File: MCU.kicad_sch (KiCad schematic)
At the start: 83 parts, among them J1 Conn_01x02_Pin, J11 Logger Connector, J12 UART Connector, J13 External UART, J14 External I2C, J15 JTAG Header, J2 Conn_01x02_Pin, J27 Conn_01x02_Pin, SW1 XRSn_button, U13 M24M01E-FMN6TP, U17 TRS3221EIPWR, U5 F280025PNS, Y2 H130B-16.000-18-3030-EXT-TR

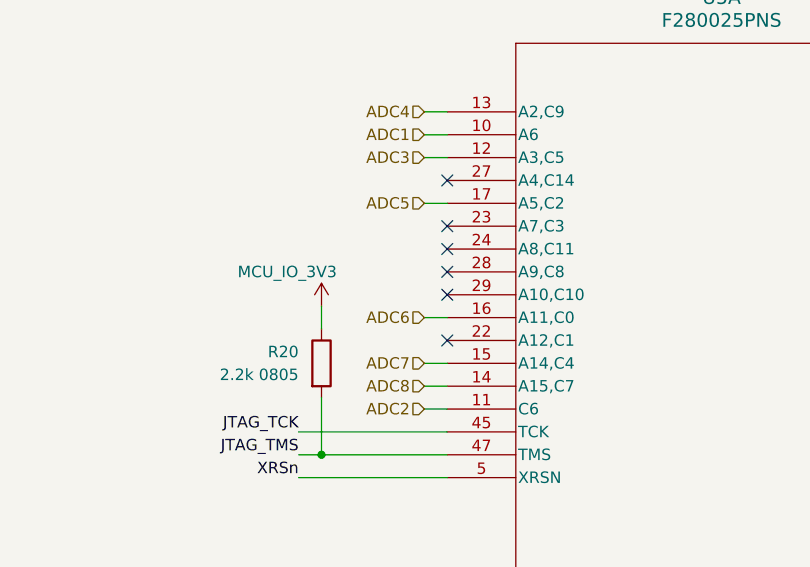
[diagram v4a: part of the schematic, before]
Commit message: re-arranged ADC channels, add voltage monitoring and connect remaining nets
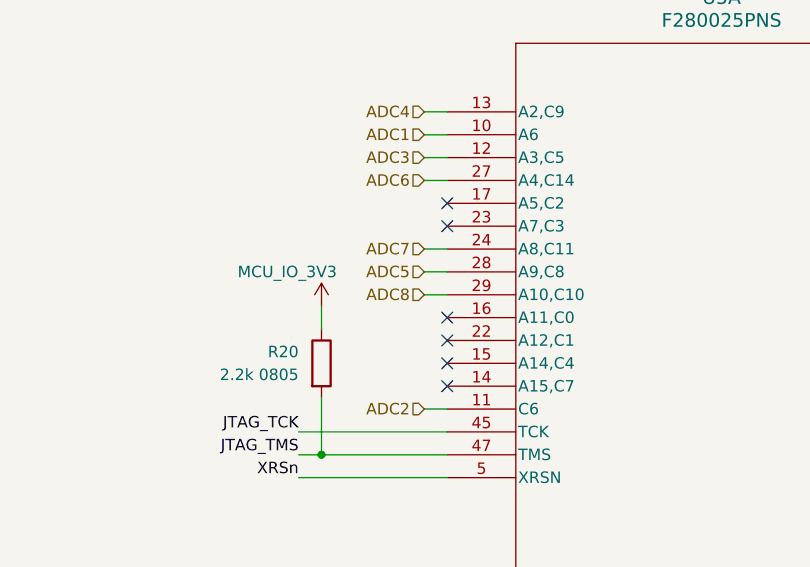
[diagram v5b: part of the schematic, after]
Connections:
- net ADC5: now also U5.28 (A9,C8); no longer U5.17 (A5,C2)
- net ADC6: now also U5.27 (A4,C14); no longer U5.16 (A11,C0)
- net ADC7: now also U5.24 (A8,C11); no longer U5.15 (A14,C4)
- net ADC8: now also U5.29 (A10,C10); no longer U5.14 (A15,C7)
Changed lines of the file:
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@@
 	)
 	(no_connect
-		(at 307.34 34.29)
+		(at 246.38 62.23)
 	)
 	(no_connect
-		(at 246.38 41.91)
+		(at 307.34 34.29)
 	)
 	(no_connect
@@
 	)
 	(no_connect
+		(at 246.38 64.77)
+	)
+	(no_connect
 		(at 97.79 208.28)
 	)
 	(no_connect
+		(at 246.38 44.45)
+	)
+	(no_connect
 		(at 246.38 59.69)
 	)
@@
 	)
 	(no_connect
-		(at 246.38 49.53)
+		(at 246.38 57.15)
 	)
 	(no_connect
@@
 	)
 	(no_connect
-		(at 246.38 52.07)
-	)
-	(no_connect
 		(at 307.34 36.83)
 	)
@@
 		(at 246.38 46.99)
 	)
-	(no_connect
-		(at 246.38 54.61)
-	)
 	(wire
 		(pts
@@
 	(wire
 		(pts
+			(xy 243.84 49.53) (xy 246.38 49.53)
+		)
+		(stroke
+			(width 0)
+			(type default)
+		)
+	)
+	(wire
+		(pts
 			(xy 170.18 48.26) (xy 175.26 48.26)
 		)
@@
 	(wire
 		(pts
+			(xy 243.84 41.91) (xy 246.38 41.91)
+		)
+		(stroke
+			(width 0)
+			(type default)
+		)
+	)
+	(wire
+		(pts
 			(xy 354.33 96.52) (xy 354.33 97.79)
 		)
@@
 	(wire
 		(pts
-			(xy 243.84 57.15) (xy 246.38 57.15)
-		)
-		(stroke
-			(width 0)
-			(type default)
-		)
-	)
-	(wire
-		(pts
 			(xy 180.34 256.54) (xy 190.5 256.54)
 		)
@@
 	(wire
 		(pts
-			(xy 243.84 44.45) (xy 246.38 44.45)
-		)
-		(stroke
-			(width 0)
-			(type default)
-		)
-	)
-	(wire
-		(pts
 			(xy 120.65 170.18) (xy 124.46 170.18)
 		)
@@
 	(wire
 		(pts
+			(xy 243.84 34.29) (xy 246.38 34.29)
+		)
+		(stroke
+			(width 0)
+			(type default)
+		)
+	)
+	(wire
+		(pts
 			(xy 307.34 74.93) (xy 309.88 74.93)
 		)
@@
 	(wire
 		(pts
+			(xy 243.84 52.07) (xy 246.38 52.07)
+		)
+		(stroke
+			(width 0)
+			(type default)
+		)
+	)
+	(wire
+		(pts
 			(xy 180.34 259.08) (xy 190.5 259.08)
 		)
@@
 	(wire
 		(pts
+			(xy 243.84 54.61) (xy 246.38 54.61)
+		)
+		(stroke
+			(width 0)
+			(type default)
+		)
+	)
+	(wire
+		(pts
 			(xy 307.34 118.11) (xy 309.88 118.11)
 		)
@@
 	(wire
 		(pts
-			(xy 243.84 62.23) (xy 246.38 62.23)
-		)
-		(stroke
-			(width 0)
-			(type default)
-		)
-	)
-	(wire
-		(pts
 			(xy 52.07 161.29) (xy 55.88 161.29)
 		)
@@
 	(wire
 		(pts
-			(xy 243.84 64.77) (xy 246.38 64.77)
-		)
-		(stroke
-			(width 0)
-			(type default)
-		)
-	)
-	(wire
-		(pts
 			(xy 52.07 177.8) (xy 52.07 180.34)
 		)
@@
 	(wire
 		(pts
-			(xy 243.84 34.29) (xy 246.38 34.29)
-		)
-		(stroke
-			(width 0)
-			(type default)
-		)
-	)
-	(wire
-		(pts
 			(xy 181.61 133.35) (xy 181.61 134.62)
 		)
@@
 	(hierarchical_label "ADC7"
 		(shape input)
-		(at 243.84 62.23 180)
+		(at 243.84 49.53 180)
 		(effects
 			(font
@@
 	(hierarchical_label "ADC8"
 		(shape input)
-		(at 243.84 64.77 180)
+		(at 243.84 54.61 180)
 		(effects
 			(font
@@
 	(hierarchical_label "ADC5"
 		(shape input)
-		(at 243.84 44.45 180)
+		(at 243.84 52.07 180)
 		(effects
 			(font
@@
 	(hierarchical_label "ADC6"
 		(shape input)
-		(at 243.84 57.15 180)
+		(at 243.84 41.91 180)
 		(effects
 			(font

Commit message: added voltage monitoring, negative HV remaining & their routing + minimal editing
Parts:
- added C49, C52, C54, C55, C56, C58, C59: 100nF, Capacitor_SMD:C_0603_1608Metric, symbol Device:C
- added C50, C51, C53, C61: 220nF, Capacitor_SMD:C_0603_1608Metric, symbol Device:C
- added R141, R149, R150: 1k, Resistor_SMD:R_0603_1608Metric, symbol Device:R
- added R142, R154: 3k, Resistor_SMD:R_0603_1608Metric, symbol Device:R
- added R143, R145, R151: 330R, Resistor_SMD:R_0603_1608Metric, symbol Device:R
- added R144, R146, R152: 500R, Resistor_SMD:R_0603_1608Metric, symbol Device:R
- added R147: 2.7k, Resistor_SMD:R_0603_1608Metric, symbol Device:R
- added R148: 2k, Resistor_SMD:R_0603_1608Metric, symbol Device:R
- added R153: 100k, Resistor_SMD:R_0603_1608Metric, symbol Device:R
- added U18, U19, U20: BZX84C3V3TS-7-F, SOT-363_DIO, symbol 2026-01-13_21-38-35:BZX84C3V3TS-7-F
- added U21: MIC920YC5-TR, MIC920YC5-TR:SOT65P210X110-5N, symbol MIC920YC5-TR:MIC920YC5-TR
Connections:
- net GND: now also C49.2, C50.2, C51.2, C52.2, C53.2, C54.2, C55.2, C56.2, C58.2, C59.2, C61.2, R141.2, R144.1, R146.1, R148.1, R152.1, R154.1, U18.1 (A1), U18.2 (A2), U18.3 (A3), U19.1 (A1), U19.2 (A2), U19.3 (A3), U20.1 (A1), U20.2 (A2), U20.3 (A3), U21.1, U21.2
- net -5v_pulse_tap: now reaches U5.14 (A15,C7)
- net -5v_pulse_tap: now also C53.1, R151.1, R152.2, U19.6 (C1)
- net 5v_pulse_tap: now reaches U5.15 (A14,C4)
- net 5v_pulse_tap: now also C50.1, R143.1, R144.2, U18.4 (C3)
- net 12V_tap: now reaches U5.16 (A11,C0)
- net 12V_tap: now also C49.1, R141.1, R142.2, U18.5 (C2)
- net 7v_vfd_tap: now reaches U5.18 (A1)
- net 7v_vfd_tap: now also C52.1, R147.1, R148.2, U19.4 (C3)
- net 5v_vfd_tap: now reaches U5.19 (A0,C15)
- net 5v_vfd_tap: now also C51.1, R145.1, R146.2, U19.5 (C2)
- net vpp_tap: now reaches U5.22 (A12,C1)
- net vpp_tap: now also C61.1, R153.2, R154.2, U20.6 (C1)
- new net: R149.1, R150.2, U21.3
- new net: R150.1, R151.2, U21.4
- new net +12V_VFD: C54.1, R142.1
- new net +5V_PULSE: C55.1, R143.2
- new net +5V_VFD: C56.1, R145.2, U21.5
- new net +7V_VFD: C58.1, R147.2
- new net -5V_PULSE: C59.1, R149.2
- new net HV_tap: U18.6 (C1)
- new net VPPA: R153.1
- new net vnn_tap: U20.5 (C2)
- no-connect marks 16 -> 11
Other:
- moved on the sheet: C112, C113, C114, C115, C116, C117, C13, C30, D1, J11, J12, J13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

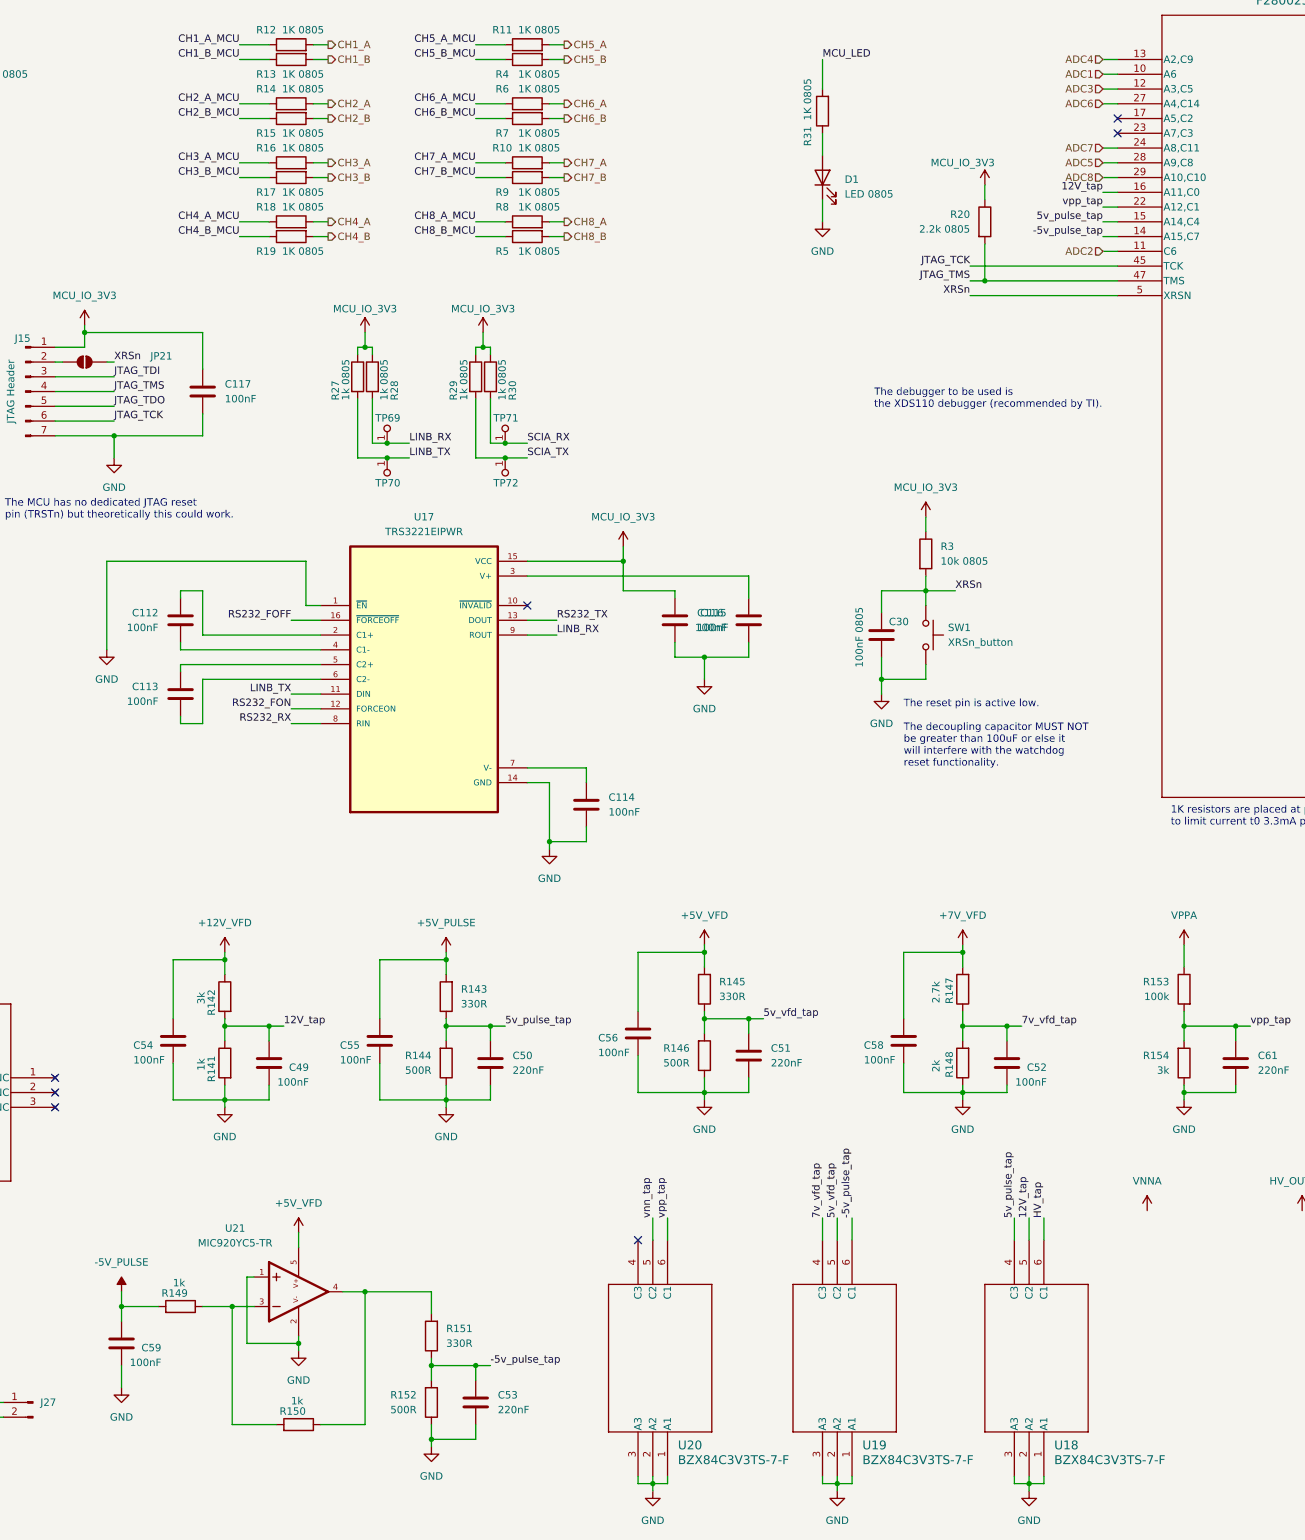
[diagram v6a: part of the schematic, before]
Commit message: finished routing YAY! only negative voltage monitoring & DRC & ERC are remaining
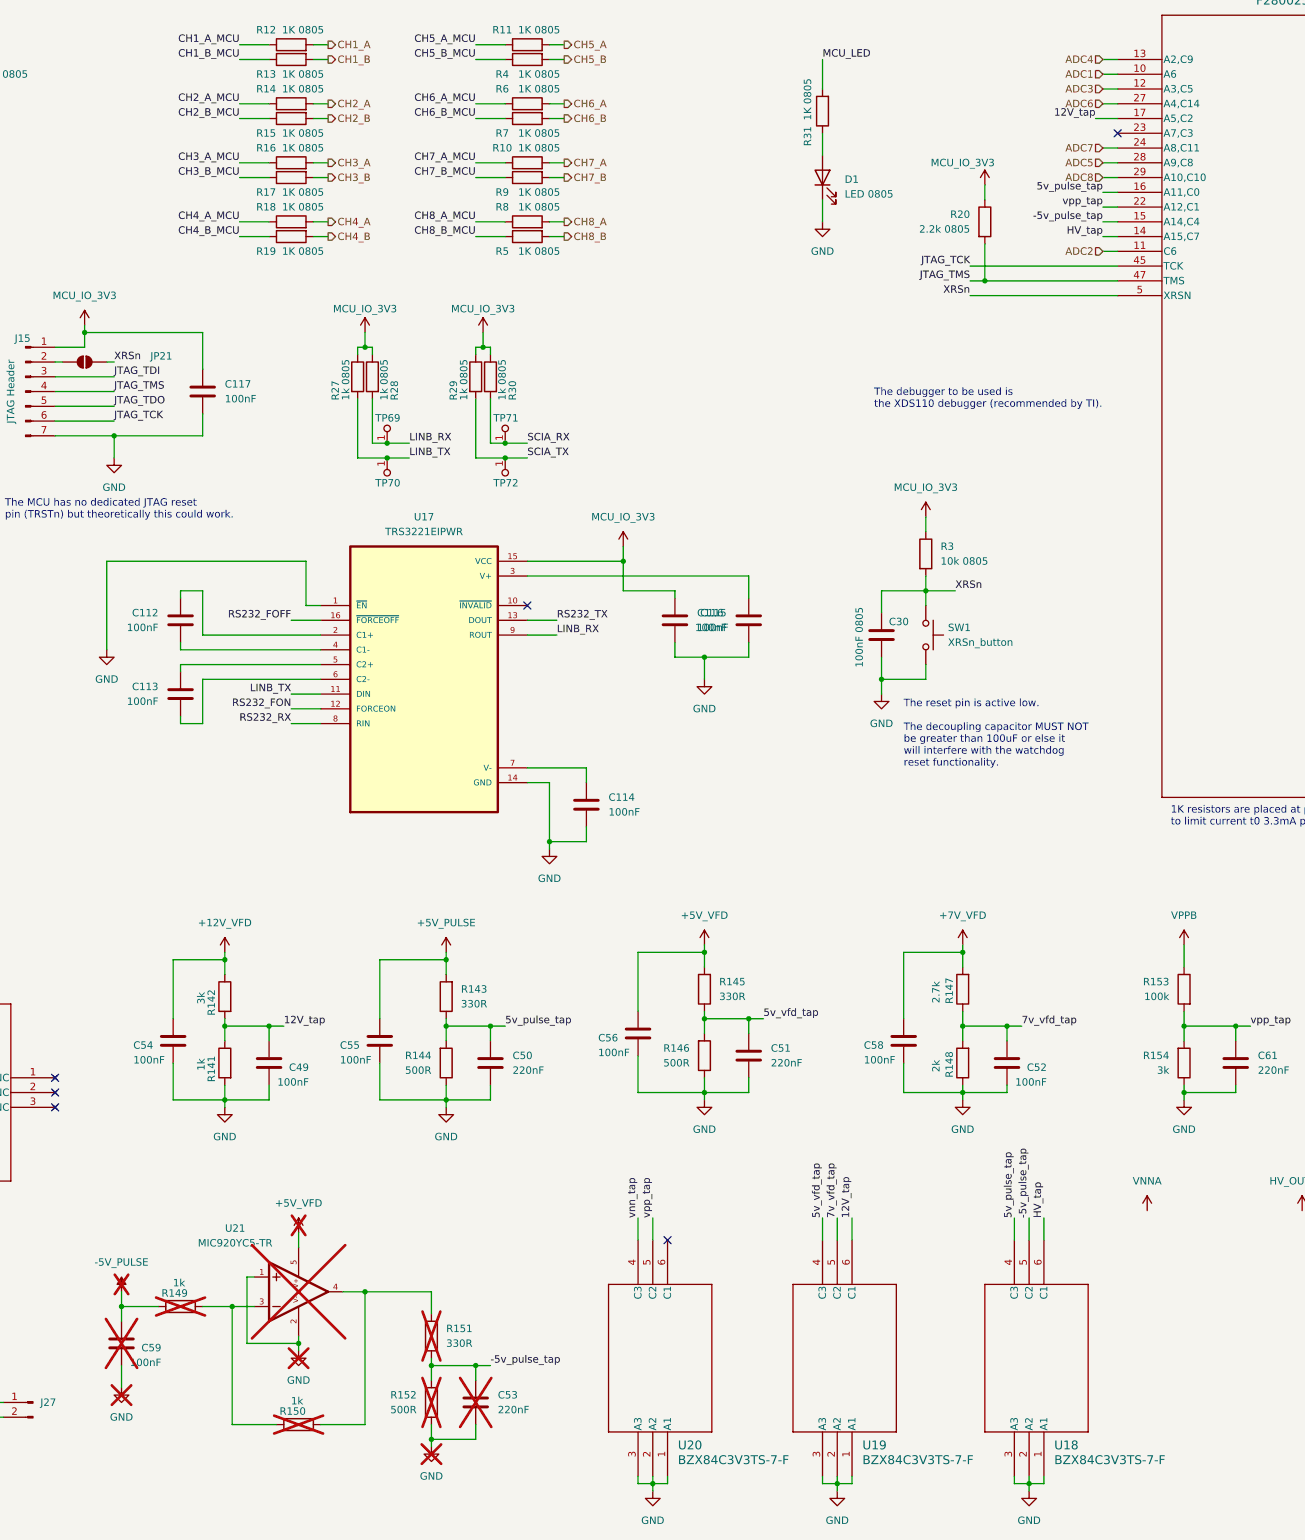
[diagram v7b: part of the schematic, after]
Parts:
- C53, C59, R149, R150, R151, R152, U21: now not fitted
- U18, U19, U20: footprint SOT-363_DIO -> BZX84C3V3TS-7-F:SOT-363_DIO
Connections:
- net -5v_pulse_tap: now also U18.5 (C2), U5.15 (A14,C4); no longer U19.6 (C1), U5.14 (A15,C7)
- net 12V_tap: now also U19.6 (C1), U5.17 (A5,C2); no longer U18.5 (C2), U5.16 (A11,C0)
- net 5v_pulse_tap: now also U5.16 (A11,C0); no longer U5.15 (A14,C4)
- net 5v_vfd_tap: now also U19.4 (C3); no longer U19.5 (C2)
- net 7v_vfd_tap: now also U19.5 (C2); no longer U19.4 (C3)
- net HV_tap: now also U5.14 (A15,C7)
- net vnn_tap: now also U20.4 (C3); no longer U20.5 (C2)
- net vpp_tap: now also U20.5 (C2); no longer U20.6 (C1)
- net VPPA renamed VPPB
- no-connect marks 11 -> 10
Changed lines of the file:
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@@
 	)
 	(no_connect
-		(at 198.12 233.68)
+		(at 179.07 124.46)
 	)
 	(no_connect
-		(at 179.07 124.46)
+		(at 203.2 233.68)
 	)
 	(no_connect
@@
 	)
 	(no_connect
-		(at 280.67 40.64)
-	)
-	(no_connect
 		(at 341.63 38.1)
 	)
@@
 	(wire
 		(pts
+			(xy 276.86 40.64) (xy 280.67 40.64)
+		)
+		(stroke
+			(width 0)
+			(type default)
+		)
+	)
+	(wire
+		(pts
 			(xy 97.79 82.55) (xy 99.06 82.55)
 		)
@@
 	(wire
 		(pts
-			(xy 203.2 229.87) (xy 203.2 233.68)
+			(xy 200.66 229.87) (xy 200.66 233.68)
 		)
 		(stroke
@@
 	(wire
 		(pts
-			(xy 200.66 229.87) (xy 200.66 233.68)
+			(xy 198.12 229.87) (xy 198.12 233.68)
 		)
 		(stroke
@@
 	)
 	(label "vpp_tap"
-		(at 203.2 229.87 90)
+		(at 200.66 229.87 90)
 		(effects
 			(font
@@
 	)
 	(label "-5v_pulse_tap"
-		(at 234.95 229.87 90)
+		(at 265.43 229.87 90)
 		(effects
 			(font
@@
 	)
 	(label "12V_tap"
-		(at 278.13 53.34 180)
+		(at 276.86 40.64 180)
 		(effects
 			(font
@@
 		)
 	)
+	(label "HV_tap"
+		(at 278.13 60.96 180)
+		(effects
+			(font
+				(size 1.27 1.27)
+			)
+			(justify right bottom)
+		)
+	)
 	(label "RS232_TX"
 		(at 44.45 243.84 0)
@@
 	)
 	(label "vnn_tap"
-		(at 200.66 229.87 90)
+		(at 198.12 229.87 90)
 		(effects
 			(font
@@
 	)
 	(label "5v_pulse_tap"
-		(at 278.13 58.42 180)
+		(at 278.13 53.34 180)
 		(effects
 			(font
@@
 	)
 	(label "12V_tap"
-		(at 265.43 229.87 90)
+		(at 234.95 229.87 90)
 		(effects
 			(font
@@
 	)
 	(label "7v_vfd_tap"
-		(at 229.87 229.87 90)
+		(at 232.41 229.87 90)
 		(effects
 			(font
@@
 	)
 	(label "5v_vfd_tap"
-		(at 232.41 229.87 90)
+		(at 229.87 229.87 90)
 		(effects
 			(font
@@
 	)
 	(label "-5v_pulse_tap"
-		(at 278.13 60.96 180)
+		(at 278.13 58.42 180)
 		(effects
 			(font
@@
 			)
 		)
-		(property "Footprint" "SOT-363_DIO"
+		(property "Footprint" "BZX84C3V3TS-7-F:SOT-363_DIO"
 			(at 267.97 233.68 0)
 			(effects
@@
 		(in_bom yes)
 		(on_board yes)
-		(dnp no)
+		(dnp yes)
 		(property "Reference" "R152"
 			(at 160.02 260.3499 0)
@@
 		(in_bom yes)
 		(on_board yes)
-		(dnp no)
+		(dnp yes)
 		(fields_autoplaced yes)
 		(property "Reference" "#PWR0193"
@@
 		(in_bom yes)
 		(on_board yes)
-		(dnp no)
+		(dnp yes)
 		(property "Reference" "U21"
 			(at 128.778 231.648 0)
@@
 		(in_bom yes)
 		(on_board yes)
-		(dnp no)
+		(dnp yes)
 		(property "Reference" "R150"
 			(at 138.684 263.144 90)
@@
 		(in_bom yes)
 		(on_board yes)
-		(dnp no)
+		(dnp yes)
 		(fields_autoplaced yes)
 		(property "Reference" "#PWR0182"
@@
 		(in_bom yes)
 		(on_board yes)
-		(dnp no)
+		(dnp yes)
 		(fields_autoplaced yes)
 		(property "Reference" "C53"
@@
 		(in_bom yes)
 		(on_board yes)
-		(dnp no)
+		(dnp yes)
 		(fields_autoplaced yes)
 		(property "Reference" "#PWR0195"
@@
 		(in_bom yes)
 		(on_board yes)
-		(dnp no)
+		(dnp yes)
 		(fields_autoplaced yes)
 		(property "Reference" "#PWR0194"
@@
 			)
 		)
-		(property "Footprint" "SOT-363_DIO"
+		(property "Footprint" "BZX84C3V3TS-7-F:SOT-363_DIO"
 			(at 234.95 233.68 0)
 			(effects
@@
 		(in_bom yes)
 		(on_board yes)
-		(dnp no)
+		(dnp yes)
 		(property "Reference" "R149"
 			(at 118.364 242.824 90)
@@
 			)
 		)
-		(property "Footprint" "SOT-363_DIO"
+		(property "Footprint" "BZX84C3V3TS-7-F:SOT-363_DIO"
 			(at 203.2 233.68 0)
 			(effects
@@
 		(in_bom yes)
 		(on_board yes)
-		(dnp no)
+		(dnp yes)
 		(fields_autoplaced yes)
 		(property "Reference" "R151"
@@
 		(in_bom yes)
 		(on_board yes)
-		(dnp no)
+		(dnp yes)
 		(fields_autoplaced yes)
 		(property "Reference" "#PWR0196"
@@
 			)
 		)
-		(property "Value" "VPPA"
+		(property "Value" "VPPB"
 			(at 292.1 177.8 0)
 			(effects
@@
 		(in_bom yes)
 		(on_board yes)
-		(dnp no)
+		(dnp yes)
 		(property "Reference" "C59"
 			(at 116.078 252.222 0)
